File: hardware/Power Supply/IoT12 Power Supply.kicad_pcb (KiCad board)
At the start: 2 copper layers, 91.4 x 73.7 mm, 14 parts, among them J1 Screw_Terminal_01x03, J2 Screw_Terminal_01x03

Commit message: Start of next iteration.
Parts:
- removed the REF** at (114.3, 97.8) (x2)
- removed the REF** at (114.3, 90.2)
- added C1: 100uF/35V, Capacitor_SMD:CP_Elec_6.3x7.7, F.Cu at (117.5, 132.7)
- added C2: 100nF, Capacitor_SMD:C_0805_2012Metric_Pad1.18x1.45mm_HandSolder, F.Cu at (120.7, 139.7)
- added C3: 100nF, Capacitor_SMD:C_0805_2012Metric_Pad1.18x1.45mm_HandSolder, F.Cu at (128.3, 123.8)
- added C4: 100uF/35V, Capacitor_SMD:CP_Elec_6.3x7.7, F.Cu at (137.2, 123.2)
- added D1: SS14, Diode_SMD:D_SMA, F.Cu at (165.1, 123.2)
- added D3: SS34, Diode_SMD:D_SMA, F.Cu at (128.3, 127.0)
- added D4: Blue, LED_SMD:LED_0805_2012Metric_Pad1.15x1.40mm_HandSolder, F.Cu at (156.2, 127.0)
- added D5: Blue, LED_SMD:LED_0805_2012Metric_Pad1.15x1.40mm_HandSolder, F.Cu at (153.7, 127.0)
- added F1: PTC 1.5A/30V, Varistor:RV_Disc_D9mm_W3.3mm_P5mm, F.Cu at (189.3, 120.0)
- added F2: PTC 0.5A/30V, Varistor:RV_Disc_D7mm_W3.4mm_P5mm, F.Cu at (189.3, 125.1)
- added J2: JST B2B-XH-A, Connector_JST:JST_XH_B2B-XH-A_1x02_P2.50mm_Vertical, F.Cu at (141.0, 132.1)
- added K1: Omron G5LE-1 24VDC, Relay_THT-fixed:Relay_SPDT_Omron-G5LE-1, F.Cu at (177.8, 122.2)
- added L1: 68uH, Inductor-fixed:L_12x12mm_H8mm, F.Cu at (129.5, 135.9)
- added Q1: MMBT2222, Package_TO_SOT_SMD:SOT-23, F.Cu at (144.8, 123.4)
- added R1: 330k, Resistor_SMD:R_0805_2012Metric_Pad1.20x1.40mm_HandSolder, F.Cu at (151.1, 123.4)
- added R3: 330k, Resistor_SMD:R_0805_2012Metric_Pad1.20x1.40mm_HandSolder, F.Cu at (166.4, 58.4)
- added R4: 330k, Resistor_SMD:R_0805_2012Metric_Pad1.20x1.40mm_HandSolder, F.Cu at (171.7, 58.4)
- added R5: 330k, Resistor_SMD:R_0805_2012Metric_Pad1.20x1.40mm_HandSolder, F.Cu at (176.5, 58.4)
- added R6: 1k, Resistor_SMD:R_0805_2012Metric_Pad1.20x1.40mm_HandSolder, F.Cu at (128.3, 118.7)
- added R7: 3k3, Resistor_SMD:R_0805_2012Metric_Pad1.20x1.40mm_HandSolder, F.Cu at (128.3, 121.3)
- added R8: 2k2, Resistor_SMD:R_0805_2012Metric_Pad1.20x1.40mm_HandSolder, F.Cu at (156.2, 121.9)
- added R9: 22k, Resistor_SMD:R_0805_2012Metric_Pad1.20x1.40mm_HandSolder, F.Cu at (153.7, 121.9)
- added TH1: 10D-15, Varistor:RV_Disc_D15.5mm_W4.5mm_P7.5mm, F.Cu at (143.9, 57.4)
- added U1: LM2596S-ADJ, Package_TO_SOT_SMD:TO-263-5_TabPin3, F.Cu at (115.6, 123.2)
- D2: value Green -> SS34; footprint LED_SMD:LED_0805_2012Metric_Pad1.15x1.40mm_HandSolder -> Diode_SMD:D_SMA
- J3: renamed from J2; value Screw_Terminal_01x03 -> JST B4B-XH-A; footprint TerminalBlock-extra:TerminalBlock_Weidmueller-PM-5.08-03-90-3.5SN-BK-BX -> Connector_JST:JST_XH_B4B-XH-A_1x04_P2.50mm_Vertical
- R2: value 4K7 -> 1k
- moved REF** 42.6 mm to (153.9, 74.3)
- moved R2 36.2 mm to (148.6, 123.4), turned to -90 degrees
- moved J3 19.3 mm to (153.8, 132.1)
- moved H2 17.8 mm to (193.0, 139.7)
- moved H4 17.8 mm to (111.8, 139.7)
- moved D2 9.94 mm to (191.8, 130.8), turned to 0 degrees
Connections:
- D2 pad 1: /Vout- -> Net-(C1-Pad1)
- H1 pad 1: Net-(H1-Pad1) -> unconnected-(H1-Pad1)
- H2 pad 1: Net-(H2-Pad1) -> unconnected-(H2-Pad1)
- H3 pad 1: Net-(H3-Pad1) -> unconnected-(H3-Pad1)
- H4 pad 1: Net-(H4-Pad1) -> unconnected-(H4-Pad1)
- J1 pad 2: /N -> /L
- J1 pad 3: /L -> /N
- J3 pad 1: Earth -> 24V_SWITCHED
- J3 pad 2: /Vout- -> +5V
- J3 pad 3: /Vout+ -> GND
- PS1 pad 1: /L -> Net-(PS1-Pad1)
- PS1 pad 3: /Vout+ -> +24V
- PS1 pad 4: /Vout- -> GND
- R2 pad 1: /Vout+ -> Net-(Q1-Pad1)
- R2 pad 2: Net-(D2-Pad2) -> 24V_ON
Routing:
- net GND: track 0.00 -> 110.0 mm, vias 0 -> 18
- net Net-(C1-Pad1): track 0.00 -> 91.6 mm
- net +5V: track 0.00 -> 57.4 mm
- net Earth: track 100.1 -> 49.2 mm
- net /SW_A: track 0.00 -> 50.4 mm, vias 0 -> 2
- net Net-(PS1-Pad1): track 0.00 -> 45.6 mm
- net /Vout-: track 42.0 -> 0.00 mm
- net /N: track 54.5 -> 13.9 mm
- net 24V_SWITCHED: track 0.00 -> 38.7 mm
- net Net-(D1-Pad1): track 0.00 -> 27.1 mm
- net /Vout+: track 22.5 -> 0.00 mm
- net 24V_ON: track 0.00 -> 21.3 mm, vias 0 -> 2
- net +24V: track 0.00 -> 17.7 mm
- net Net-(D3-Pad1): track 0.00 -> 16.0 mm
- net Net-(R6-Pad2): track 0.00 -> 8.55 mm
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- added copper zone on B.Cu, net GND
- added copper zone on F.Cu, net GND
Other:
- board size 91.4 x 73.7 mm -> 91.4 x 91.4 mm
- net class Default removed
- board text added: "+24V"
- board text added: "+24V ON"
- board text added: "+5V"
- board text added: "1M electro static discharge path to earth."
- board text added: "AC/L"
- board text added: "AC/N"
- board text added: "E"
- board text added: "Earth, AC/L, AC/N -->"
- board text added: "GND"
- board text added: "IoT12 power supply, 2022-12-20, V1.2 Mean Well MPM-90-24 Input: 100-240VAC, 1.9A 50/60Hz Output: 24V, 3.75A, 90W. https://github.com/atoomnetmarc/IoT12 Apache License, Version 2.0"
- board text added: "L"
- board text added: "N"
- board text added: "Power switch"
- board text removed: "ACL"
- board text removed: "ACN"
- board text removed: "EARTH, -, +"
- board text removed: "EARTH, AC/N, AC/L"
- board text removed: "IoT12 Power Supply 2021-10-21, V1.1"
- board text removed: "Recommended power supply module: Mean Well MPM-90-24 Input: 80-264VAC, 113-370VDC. Output: 24V, 3.75A, 90W. https://github.com/atoomnetmarc/IoT12-hardware Apache License, Version 2.0"
- board text removed: "This PCB is not safe to use. Use at your own risk. When powered on it becomes deadly when touched or could set your house on fire when left unsupervised."
- board text removed: "Vout+"
- board text removed: "Vout-"

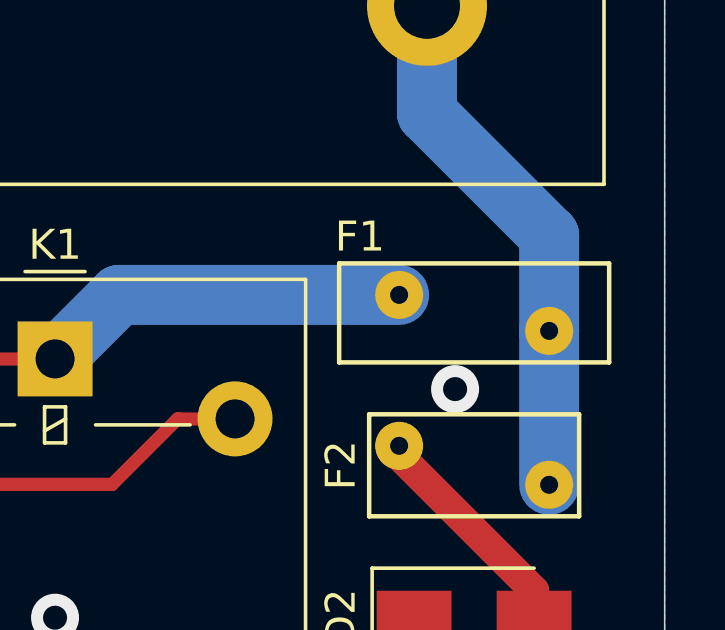
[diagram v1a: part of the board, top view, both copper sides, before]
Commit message: Add PDF. Enlarge F1 pad size.
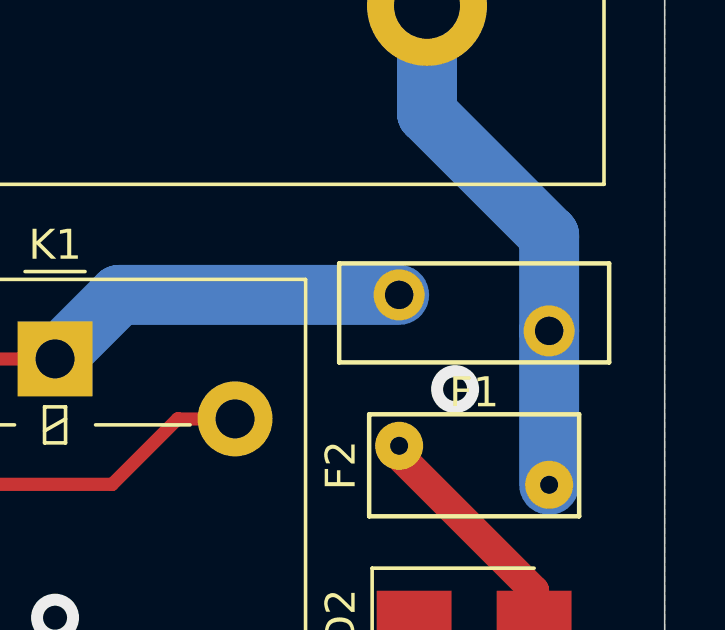
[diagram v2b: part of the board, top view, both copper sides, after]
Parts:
- F1: footprint Varistor:RV_Disc_D9mm_W3.3mm_P5mm -> Varistor-extra:RV_Disc_D9mm_W3.3mm_P5mm
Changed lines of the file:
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@@
     )
   )
-  (footprint "Varistor:RV_Disc_D9mm_W3.3mm_P5mm" (layer "F.Cu")
+  (footprint "Varistor-extra:RV_Disc_D9mm_W3.3mm_P5mm" (layer "F.Cu")
     (at 189.27 120.05)
     (descr "Varistor, diameter 9mm, width 3.3mm, pitch 5mm")
@@
     (property "Sheetname" "")
     (attr through_hole)
-    (fp_text reference "F1" (at -1.31 -1.94) (layer "F.SilkS")
+    (fp_text reference "F1" (at 2.5 3.25) (layer "F.SilkS")
       (effects (font (size 1 1) (thickness 0.15)))
     )
@@
       (effects (font (size 1 1) (thickness 0.15)))
     )
+    (fp_line (start -2 -1.05) (end 7 -1.05) (layer "F.SilkS") (width 0.15))
+    (fp_line (start -2 -1.05) (end -2 2.25) (layer "F.SilkS") (width 0.15))
     (fp_line (start 7 -1.05) (end 7 2.25) (layer "F.SilkS") (width 0.15))
     (fp_line (start -2 2.25) (end 7 2.25) (layer "F.SilkS") (width 0.15))
-    (fp_line (start -2 -1.05) (end 7 -1.05) (layer "F.SilkS") (width 0.15))
-    (fp_line (start -2 -1.05) (end -2 2.25) (layer "F.SilkS") (width 0.15))
     (fp_line (start 7.25 -1.3) (end 7.25 2.5) (layer "F.CrtYd") (width 0.05))
-    (fp_line (start -2.25 2.5) (end 7.25 2.5) (layer "F.CrtYd") (width 0.05))
     (fp_line (start -2.25 -1.3) (end -2.25 2.5) (layer "F.CrtYd") (width 0.05))
     (fp_line (start -2.25 -1.3) (end 7.25 -1.3) (layer "F.CrtYd") (width 0.05))
+    (fp_line (start -2.25 2.5) (end 7.25 2.5) (layer "F.CrtYd") (width 0.05))
+    (fp_line (start -2 -1.05) (end -2 2.25) (layer "F.Fab") (width 0.1))
+    (fp_line (start 7 -1.05) (end 7 2.25) (layer "F.Fab") (width 0.1))
     (fp_line (start -2 2.25) (end 7 2.25) (layer "F.Fab") (width 0.1))
     (fp_line (start -2 -1.05) (end 7 -1.05) (layer "F.Fab") (width 0.1))
-    (fp_line (start 7 -1.05) (end 7 2.25) (layer "F.Fab") (width 0.1))
-    (fp_line (start -2 -1.05) (end -2 2.25) (layer "F.Fab") (width 0.1))
-    (pad "1" thru_hole circle (at 0 0) (size 1.6 1.6) (drill 0.6) (layers *.Cu *.Mask)
+    (pad "1" thru_hole circle (at 0 0) (size 1.7 1.7) (drill 0.95) (layers *.Cu *.Mask)
       (net 13 "Net-(D1-Pad1)") (pintype "passive"))
-    (pad "2" thru_hole circle (at 5 1.2) (size 1.6 1.6) (drill 0.6) (layers *.Cu *.Mask)
+    (pad "2" thru_hole circle (at 5 1.2) (size 1.7 1.7) (drill 0.95) (layers *.Cu *.Mask)
       (net 16 "+24V") (pintype "passive"))
     (model "${KICAD6_3DMODEL_DIR}/Varistor.3dshapes/RV_Disc_D9mm_W3.3mm_P5mm.wrl"

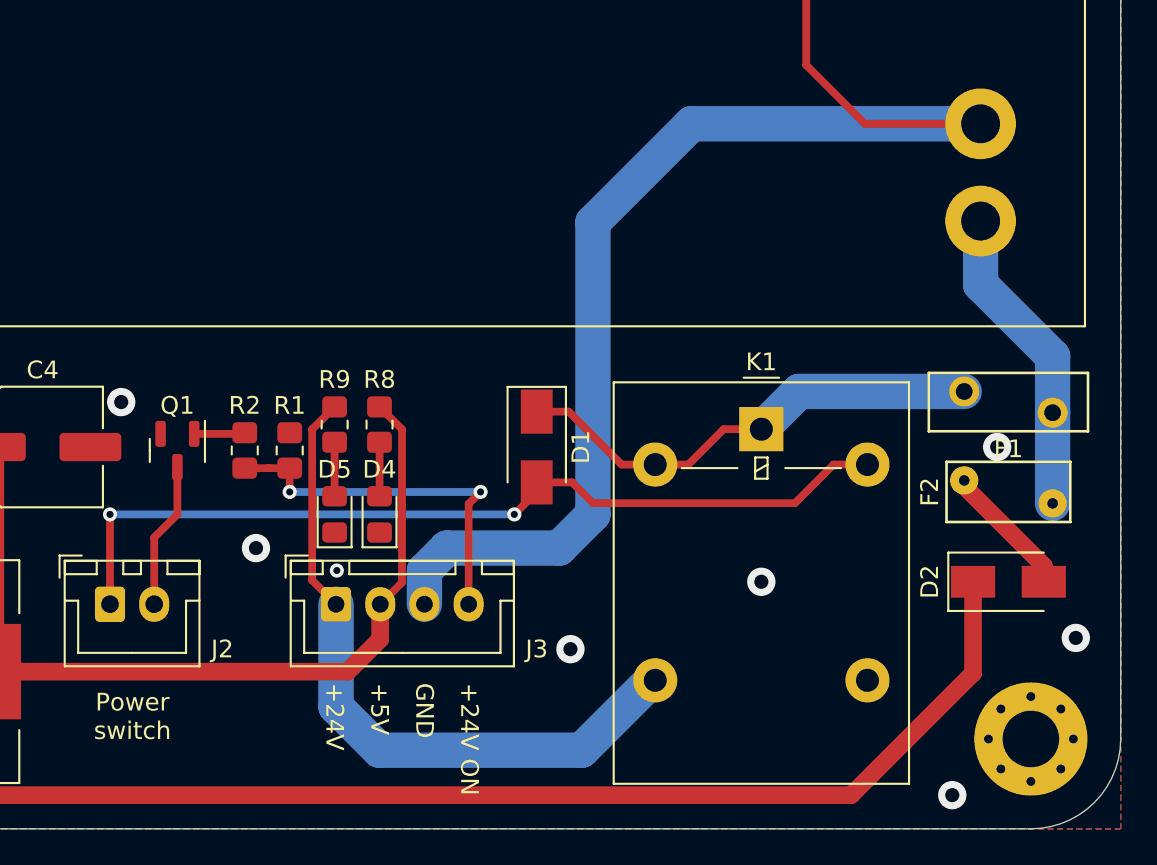
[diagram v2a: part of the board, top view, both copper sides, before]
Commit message: Make more room around F1.
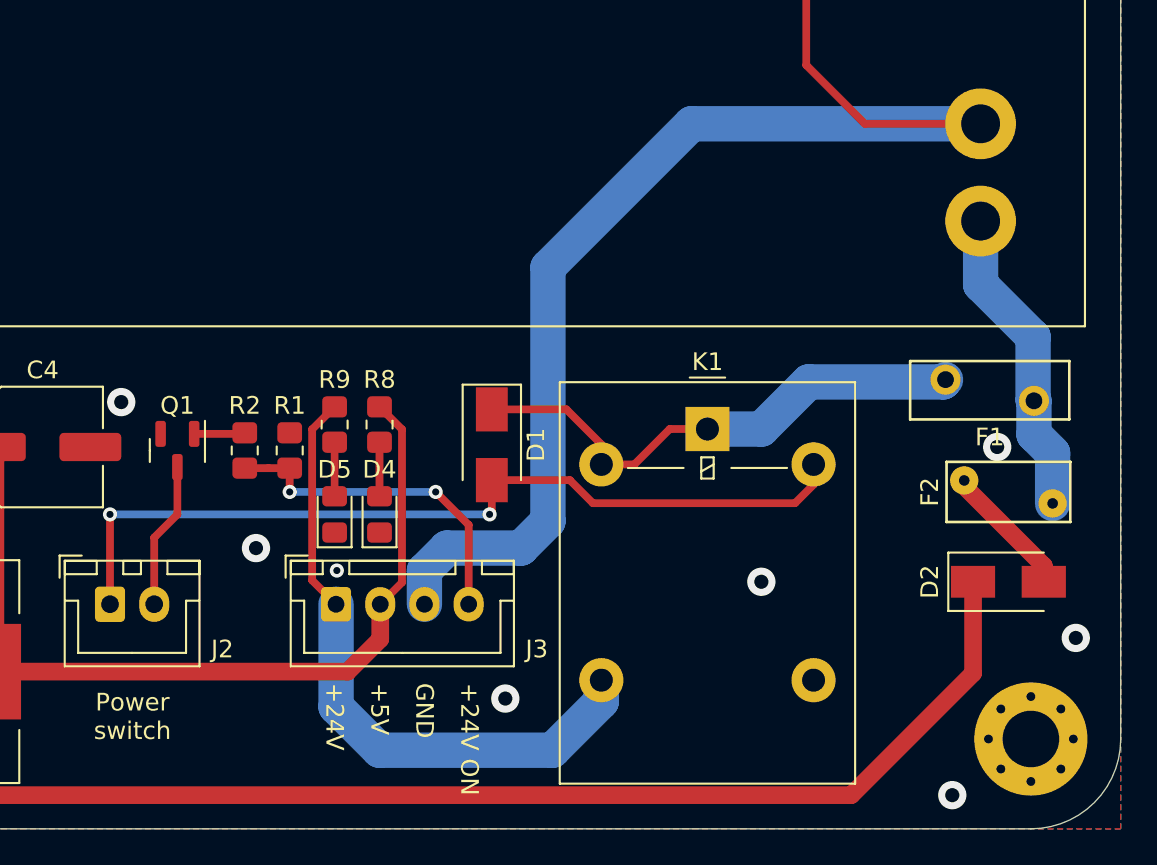
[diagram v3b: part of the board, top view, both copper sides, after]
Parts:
- moved K1 3.05 mm to (174.8, 122.2)
- moved D1 2.54 mm to (162.6, 123.1)
- moved F1 1.25 mm to (188.2, 119.4)
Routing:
- net Net-(D1-Pad1): track 27.1 -> 29.6 mm
- net 24V_SWITCHED: track 38.7 -> 36.4 mm
- net 24V_ON: track 21.3 -> 19.3 mm
- net /SW_A: track 50.4 -> 48.8 mm
- net GND: track 110.0 -> 108.7 mm

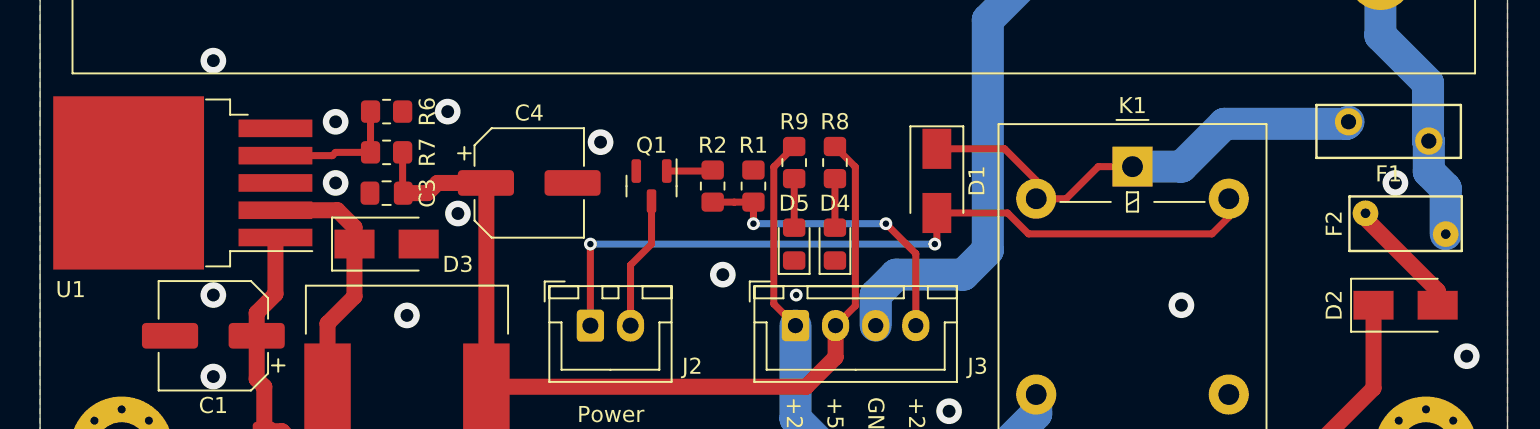
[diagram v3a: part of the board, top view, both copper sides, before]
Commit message: Update Power Supply project to Kicad 7.0.2
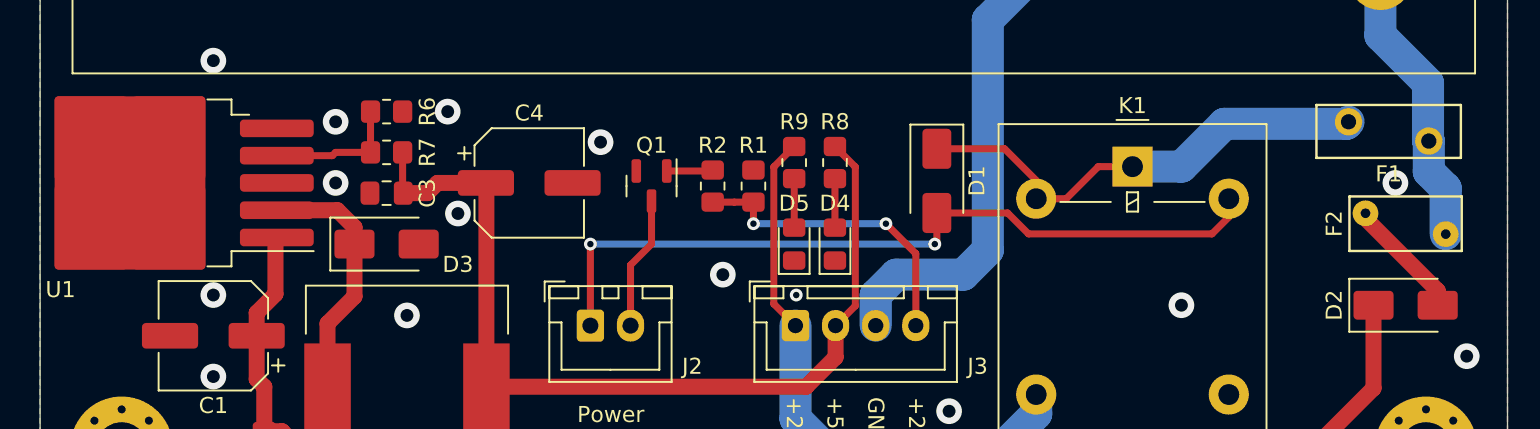
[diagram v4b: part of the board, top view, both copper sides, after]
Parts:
- K1: footprint Relay_THT-fixed:Relay_SPDT_Omron-G5LE-1 -> Relay_THT:Relay_SPDT_Omron-G5LE-1
- moved U1 1.79 mm to (113.8, 123.2)
